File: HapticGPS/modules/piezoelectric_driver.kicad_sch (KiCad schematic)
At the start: 12 parts, among them IC1 BOS1921CQR, J2 PZ

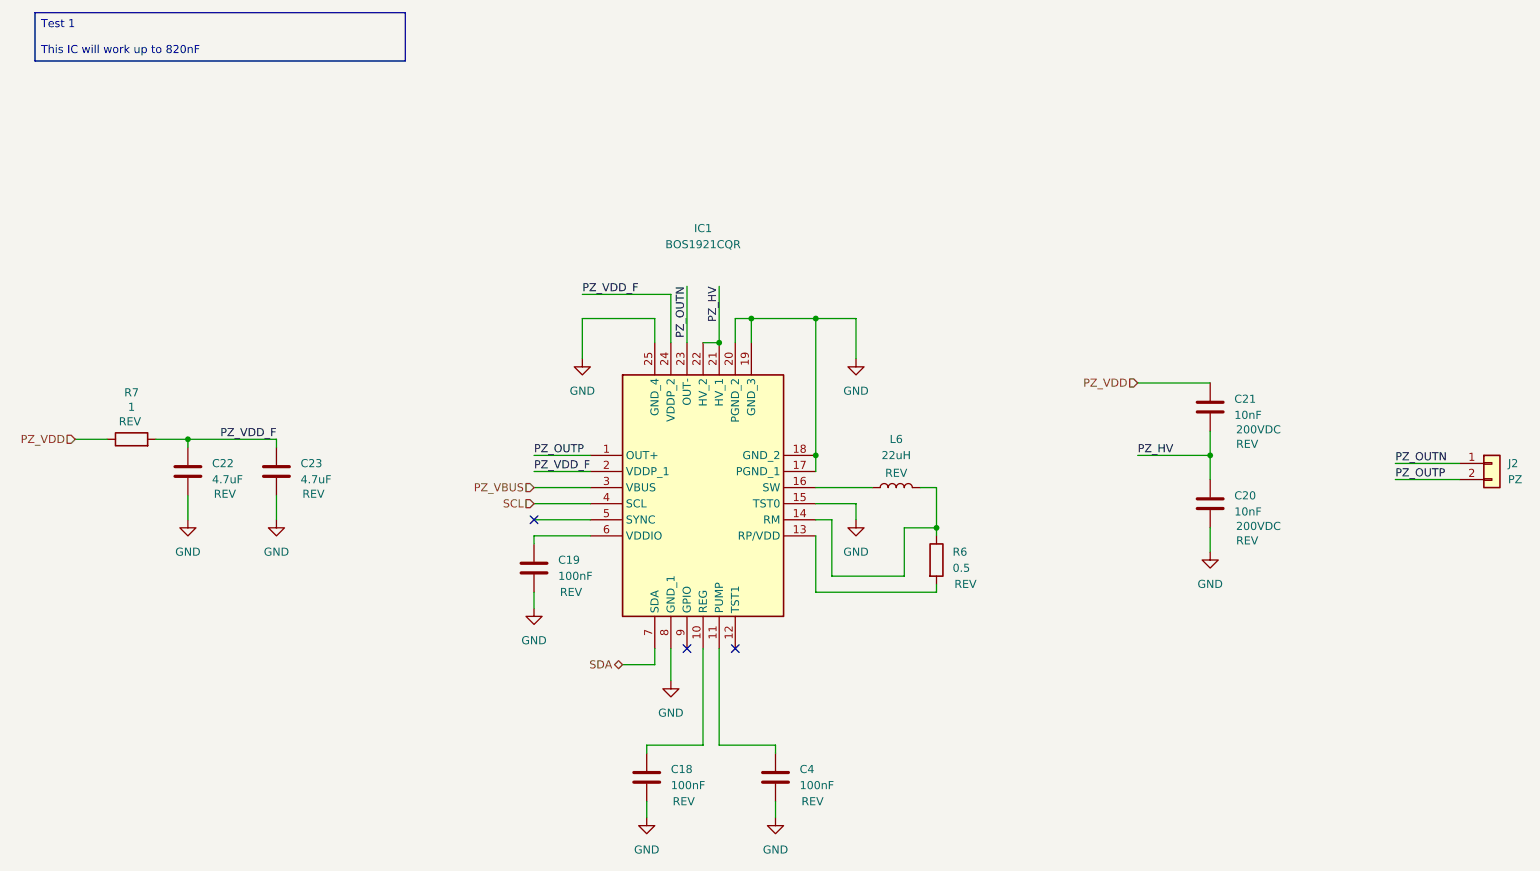
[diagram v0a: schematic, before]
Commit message: eliminating GPS, and second piezo driver
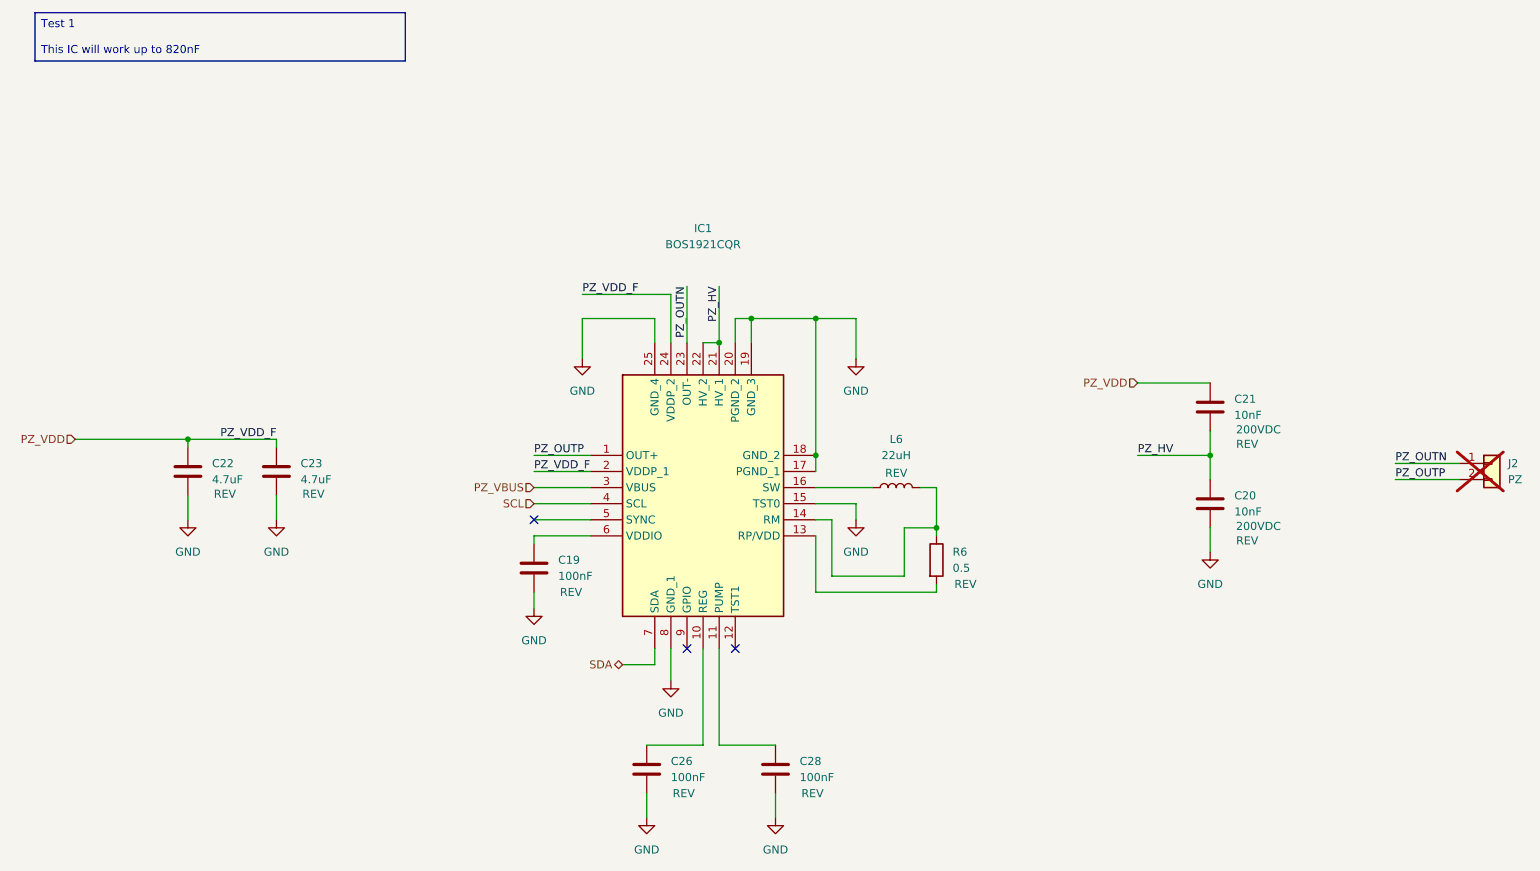
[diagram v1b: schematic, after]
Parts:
- removed C18, C4: 100nF, Capacitor_SMD:C_0603_1608Metric, symbol Device:C
- removed R7: 1, Resistor_SMD:R_0805_2012Metric, symbol Device:R
- added C26, C28: 100nF, Capacitor_SMD:C_0402_1005Metric, symbol Device:C
- IC1: Manufacturer (none) -> Boreas Technologies; Number Part (none) -> BOS1921CQR; Provider (none) -> Digikey
- J2: now not fitted; now left out of the parts list
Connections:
- net PZ_VDD_F is gone; now on net PZ_VDD: C22.2, C23.2, IC1.2 (VDDP_1), IC1.24 (VDDP_2)
- net GND: now also C26.2, C28.2
- net at IC1.10 (REG): now also C26.1
- net at IC1.11 (PUMP): now also C28.1
